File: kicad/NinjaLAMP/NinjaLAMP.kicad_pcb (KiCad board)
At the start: 2 copper layers, 84.5 x 30 mm, 37 parts, among them J1 Barrel_Jack_Switch, J2 Conn_01x05_Male, Q1 BSP89, Q2 BSP89, SW0 DIP-BUTTON_2P-6.0X3.0X4.3MM_, SW1 DIP-BUTTON_2P-6.0X3.0X4.3MM_, SW2 DIP-BUTTON_2P-6.0X3.0X4.3MM_, U1 SeeeduinoXIAO, U2 PMIC-CJ78M05_TO-252_

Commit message: add 3dprint data
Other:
- board text added: "84.5x30mm"
- board text removed: "82x30mm"

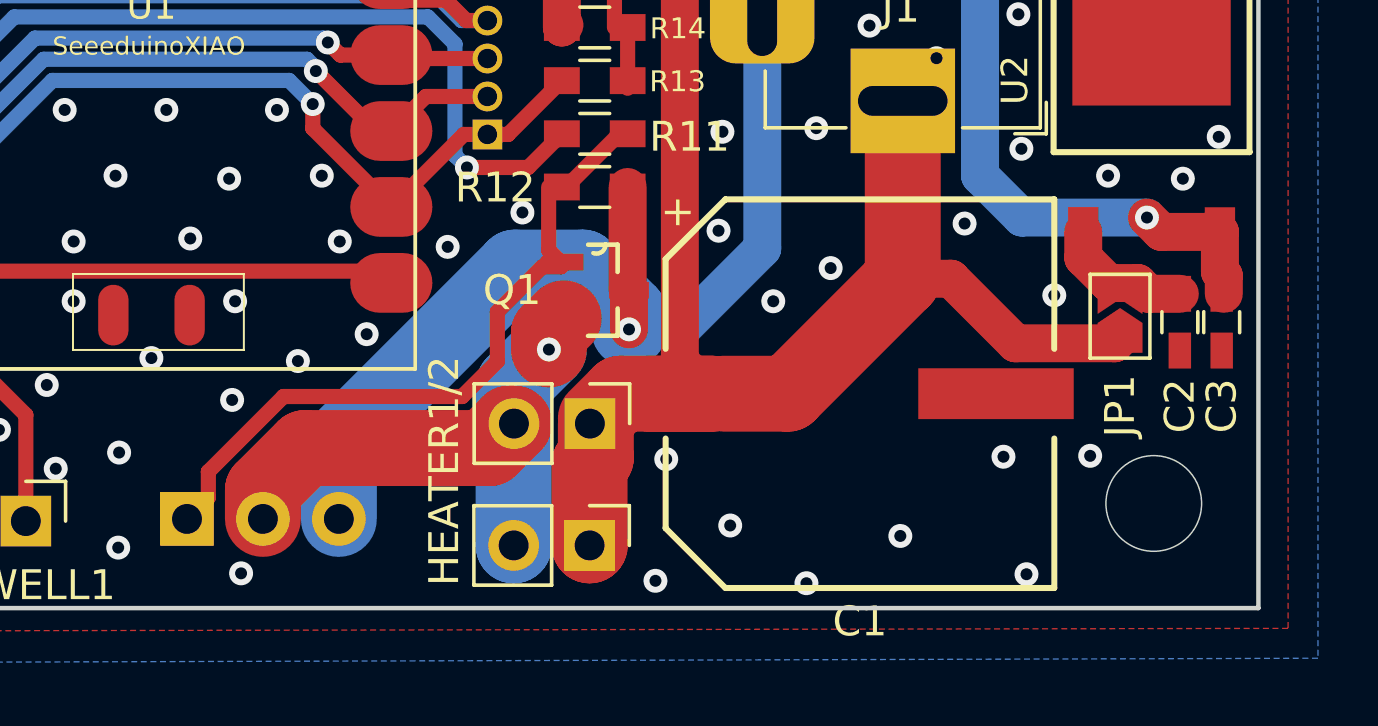
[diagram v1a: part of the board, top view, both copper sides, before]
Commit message: bigger footprint for polcap
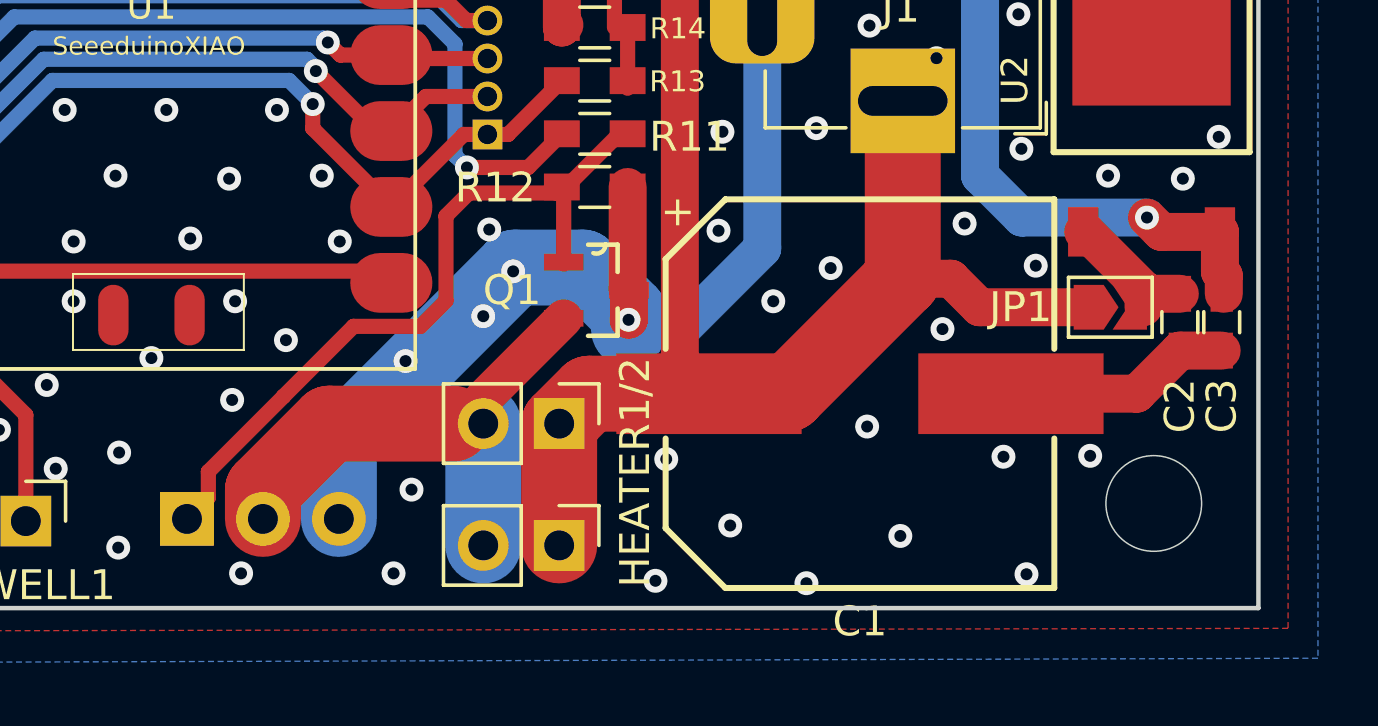
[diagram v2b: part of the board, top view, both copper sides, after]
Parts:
- moved HEATER2 1.03 mm to (171.1, 111.4)
- moved HEATER1 1.02 mm to (171.1, 115.4)
- moved JP1 0.44 mm to (189.6, 107.5), turned to 0 degrees
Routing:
- net GND: track 68.8 -> 76.1 mm, vias 166 -> 171
- net +12V: track 51.8 -> 49.2 mm
- net /Q2: track 19.3 -> 18.0 mm, vias 1 -> 0
- net /Q1: track 24.0 -> 24.9 mm

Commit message: add todo memo
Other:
- board text added: "TODO : Bigger pad for heater / Use 4 in 1 resistor for tacts with R12 / Place tacts next to LCD"
